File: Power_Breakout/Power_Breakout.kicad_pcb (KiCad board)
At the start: 2 copper layers, 89.7 x 26.3 mm, 5 parts, among them J1 12v Out, J2 GND Out, J3 PS Conn, SW1 ON

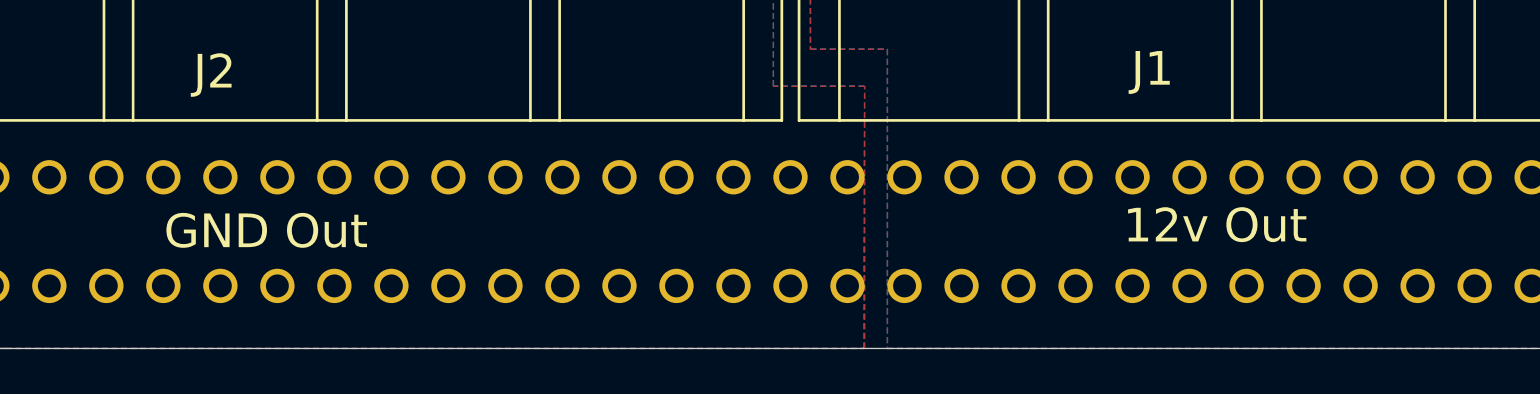
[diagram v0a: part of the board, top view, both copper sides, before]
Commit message: added silkscreen with board information
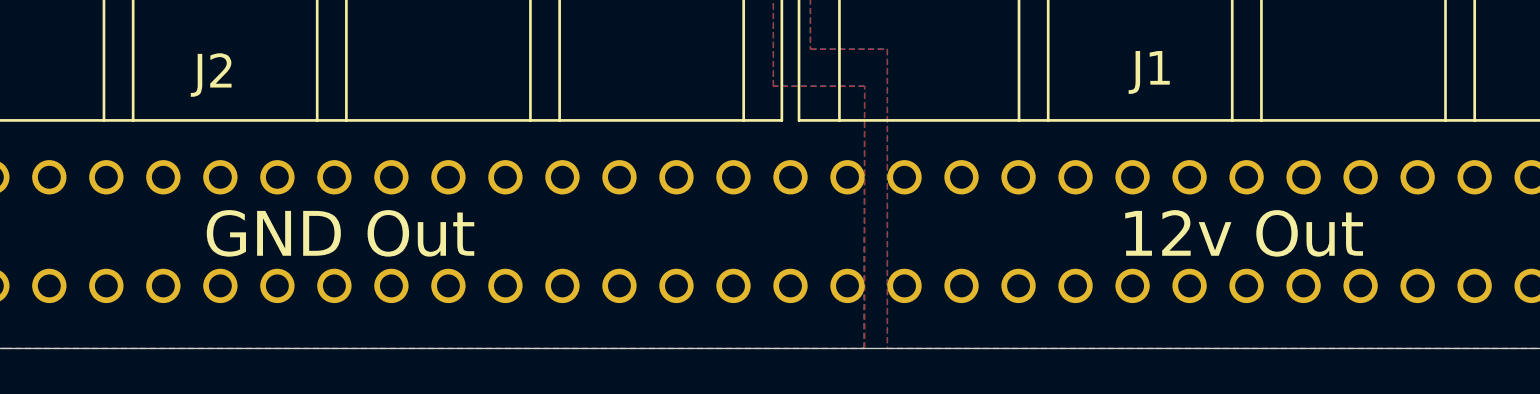
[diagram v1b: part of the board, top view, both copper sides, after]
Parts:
- added REF**: KiCad-Logo2_5mm_SilkScreen, Symbol:KiCad-Logo2_5mm_SilkScreen, B.Cu at (137.7, 149.3)
- added REF**: OSHW-Logo2_7.3x6mm_SilkScreen, Symbol:OSHW-Logo2_7.3x6mm_SilkScreen, B.Cu at (192.1, 149.2)
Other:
- board text added: "HP Power Breakout v1 By Scott Hanson"

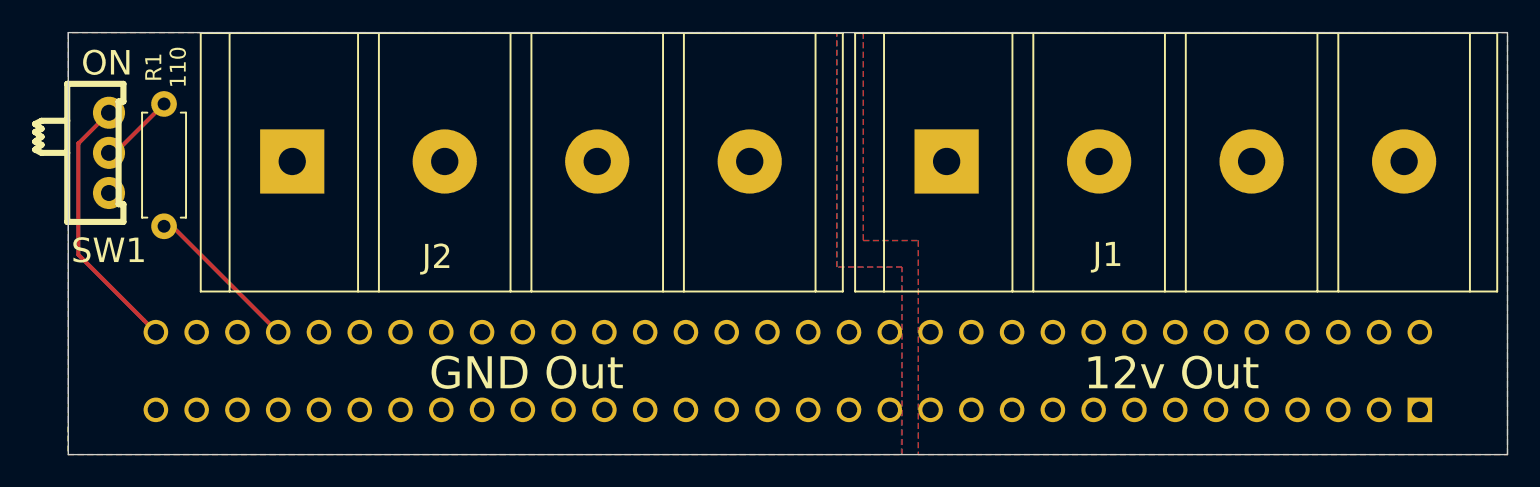
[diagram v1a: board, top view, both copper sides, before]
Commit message: made the PCB a little smaller
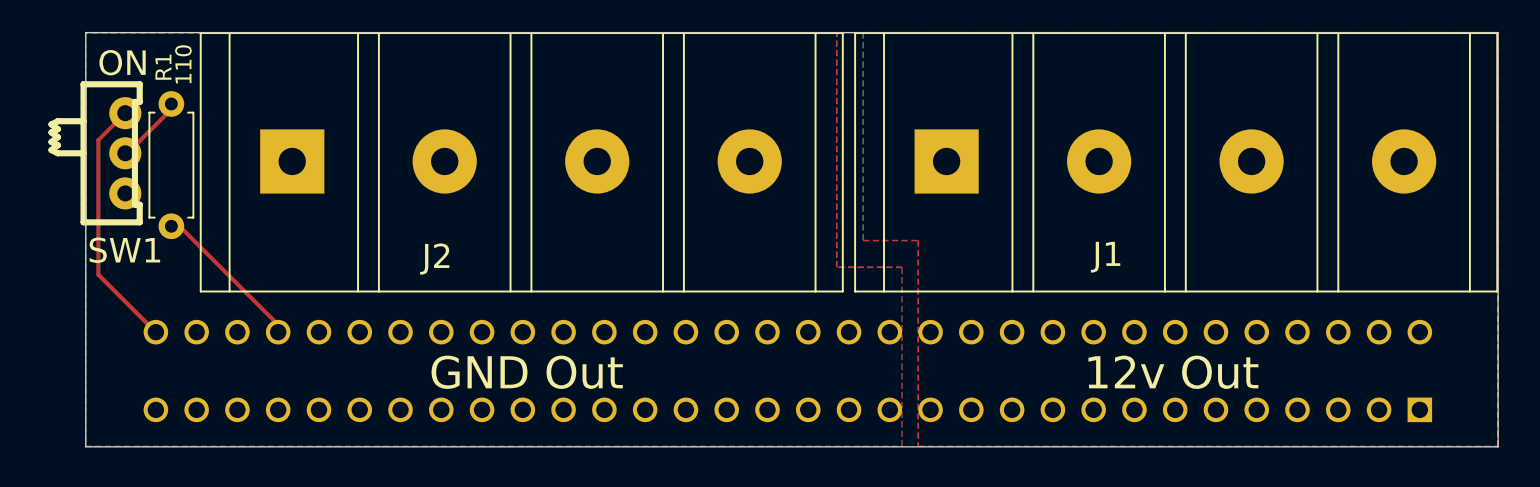
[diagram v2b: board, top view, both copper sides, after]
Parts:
- moved SW1 1.02 mm to (117.1, 143.8)
- moved R1 0.46 mm to (120.0, 148.3)
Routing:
- net Net-(J3-Pad33): track 16.5 -> 15.8 mm
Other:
- board size 89.7 x 26.3 mm -> 88 x 25.8 mm
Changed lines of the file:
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@@
     (thickness 1.6)
     (drawings 8)
-    (tracks 8)
+    (tracks 10)
     (zones 0)
     (modules 7)
@@
   )
   (module switch:switch_mmp122-r (layer F.Cu)
-    (at 116.078 143.764 270)
+    (at 117.094 143.7894 270)
     (descr "Knitter MMP122-R")
     (fp_text reference SW1 (at 6.096 0 180) (layer F.SilkS)
@@
   )
   (module Resistor_THT:R_Axial_DIN0207_L6.3mm_D2.5mm_P7.62mm_Horizontal (layer F.Cu)
-    (at 119.507 148.336 90)
+    (at 119.9642 148.336 90)
     (descr "Resistor, Axial_DIN0207 series, Axial, Horizontal, pin pitch=7.62mm, 0.25W = 1/4W, length*diameter=6.3*2.5mm^2, http://cdn-reichelt.de/documents/datenblatt/B400/1_4W%23YAG.pdf")
     (tags "Resistor Axial_DIN0207 series Axial Horizontal pin pitch 7.62mm 0.25W = 1/4W length 6.3mm diameter 2.5mm")
-    (fp_text reference R1 (at 9.906 -0.635 90) (layer F.SilkS)
+    (fp_text reference R1 (at 9.906 -0.4572 90) (layer F.SilkS)
       (effects (font (size 1 1) (thickness 0.15)))
     )
-    (fp_text value 110 (at 9.906 0.889 90) (layer F.SilkS)
+    (fp_text value 110 (at 10.0584 0.7874 90) (layer F.SilkS)
       (effects (font (size 1 1) (thickness 0.15)))
     )
@@
     (effects (font (size 1.5 1.5) (thickness 0.25)) (justify mirror))
   )
-  (gr_text ON (at 115.951 138.176) (layer B.SilkS)
+  (gr_text ON (at 116.967 138.2014) (layer B.SilkS)
     (effects (font (size 1.5 1.5) (thickness 0.3)) (justify mirror))
   )
@@
     (effects (font (size 2.5 2.5) (thickness 0.5)) (justify mirror))
   )
-  (gr_line (start 113.538 136.271) (end 113.538 162.56) (layer Edge.Cuts) (width 0.05))
-  (gr_line (start 203.2 136.271) (end 113.538 136.271) (layer Edge.Cuts) (width 0.05))
-  (gr_line (start 203.2 162.56) (end 203.2 136.271) (layer Edge.Cuts) (width 0.05))
-  (gr_line (start 113.538 162.56) (end 203.2 162.56) (layer Edge.Cuts) (width 0.05))
-  (segment (start 120.022 148.336) (end 126.619 154.933) (width 0.25) (layer F.Cu) (net 5))
-  (segment (start 119.507 148.336) (end 120.022 148.336) (width 0.25) (layer F.Cu) (net 5))
+  (gr_line (start 114.6302 136.271) (end 114.6302 162.0774) (layer Edge.Cuts) (width 0.05))
+  (gr_line (start 202.6158 136.271) (end 114.6302 136.271) (layer Edge.Cuts) (width 0.05))
+  (gr_line (start 202.6158 162.0774) (end 202.6158 136.271) (layer Edge.Cuts) (width 0.05))
+  (gr_line (start 114.6302 162.0774) (end 202.6158 162.0774) (layer Edge.Cuts) (width 0.05))
+  (segment (start 120.4792 148.336) (end 127.0762 154.933) (width 0.25) (layer F.Cu) (net 5))
+  (segment (start 119.9642 148.336) (end 120.4792 148.336) (width 0.25) (layer F.Cu) (net 5))
+  (segment (start 115.4176 151.3516) (end 118.234001 154.168001) (width 0.25) (layer F.Cu) (net 8))
   (segment (start 118.234001 154.168001) (end 118.999 154.933) (width 0.25) (layer F.Cu) (net 8))
-  (segment (start 114.173 150.107) (end 118.234001 154.168001) (width 0.25) (layer F.Cu) (net 8))
-  (segment (start 116.078 141.26464) (end 114.173 143.16964) (width 0.25) (layer F.Cu) (net 8))
-  (segment (start 114.173 143.16964) (end 114.173 150.107) (width 0.25) (layer F.Cu) (net 8))
-  (segment (start 116.459 143.764) (end 119.507 140.716) (width 0.25) (layer F.Cu) (net 15))
-  (segment (start 116.078 143.764) (end 116.459 143.764) (width 0.25) (layer F.Cu) (net 15))
+  (segment (start 117.094 141.29004) (end 115.4176 142.96644) (width 0.25) (layer F.Cu) (net 8))
+  (segment (start 115.4176 142.96644) (end 115.4176 151.3516) (width 0.25) (layer F.Cu) (net 8))
+  (segment (start 116.5352 143.764) (end 116.9162 143.764) (width 0.25) (layer F.Cu) (net 15))
+  (segment (start 119.9642 141.0462) (end 119.9642 140.716) (width 0.25) (layer F.Cu) (net 15))
+  (segment (start 117.094 143.7894) (end 117.221 143.7894) (width 0.25) (layer F.Cu) (net 15))
+  (segment (start 117.221 143.7894) (end 119.9642 141.0462) (width 0.25) (layer F.Cu) (net 15))
   (zone (net 1) (net_name +12V) (layer B.Cu) (hatch edge 0.508)
     (connect_pads (clearance 0.15))
@@
     (polygon
       (pts
-        (xy 203.2 136.271) (xy 163.068 136.271) (xy 163.068 149.225) (xy 166.497 149.225) (xy 166.497 162.56)
-        (xy 203.2 162.56)
+        (xy 202.6158 136.271) (xy 163.068 136.271) (xy 163.068 149.225) (xy 166.497 149.225) (xy 166.497 162.052)
+        (xy 202.6158 162.052)
       )
     )
@@
     (polygon
       (pts
-        (xy 203.2 136.271) (xy 163.068 136.271) (xy 163.068 149.225) (xy 166.497 149.225) (xy 166.497 162.56)
-        (xy 203.2 162.56)
+        (xy 202.6158 136.271) (xy 163.068 136.271) (xy 163.068 149.225) (xy 166.497 149.225) (xy 166.497 162.052)
+        (xy 202.6158 162.052)
       )
     )
@@
     (polygon
       (pts
-        (xy 165.481 150.876) (xy 161.417 150.876) (xy 161.417 136.271) (xy 113.538 136.271) (xy 113.504469 162.56)
-        (xy 121.886469 162.56) (xy 127.220469 162.56) (xy 165.447469 162.56)
+        (xy 165.481 150.9014) (xy 161.417 150.9014) (xy 161.417 136.2964) (xy 114.6302 136.2964) (xy 114.6302 162.052)
+        (xy 165.481 162.052)
       )
     )
@@
     (polygon
       (pts
-        (xy 165.481 150.876) (xy 161.417 150.876) (xy 161.417 136.271) (xy 113.538 136.271) (xy 113.538 162.56)
-        (xy 165.481 162.56)
+        (xy 165.481 150.876) (xy 161.417 150.876) (xy 161.417 136.271) (xy 114.6302 136.271) (xy 114.6302 162.052)
+        (xy 165.481 162.052)
       )
     )

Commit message: added more text to silkscreen
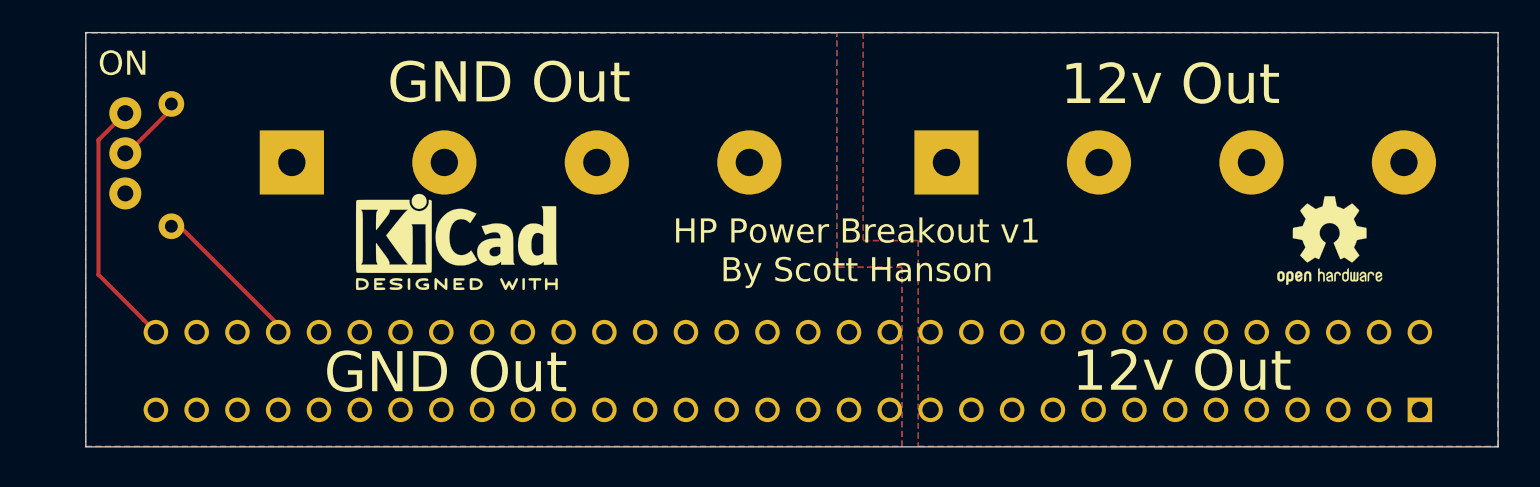
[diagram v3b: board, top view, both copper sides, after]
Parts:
- J1, J2, R1, SW1: moved to B.Cu
- REF** (x2): moved to F.Cu
- moved J2 16.1 mm to (121.8, 136.3)
- moved J1 16.1 mm to (162.5, 136.3)
- turned REF** to 0 degrees (x2)
- turned SW1 to 90 degrees
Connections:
- SW1 pad 1: Net-(J3-Pad33) -> Net-(SW1-Pad1)
- SW1 pad 3: (no net) -> Net-(J3-Pad33)
